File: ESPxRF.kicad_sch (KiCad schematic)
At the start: 22 parts, among them J1 Conn_Coaxial, J2 USB_C_Receptacle_USB2.0, U1 ESP32-S3, U2 NRF24L01, U3 NCP115ASN330T2G, U4 USBLC6-2SC6

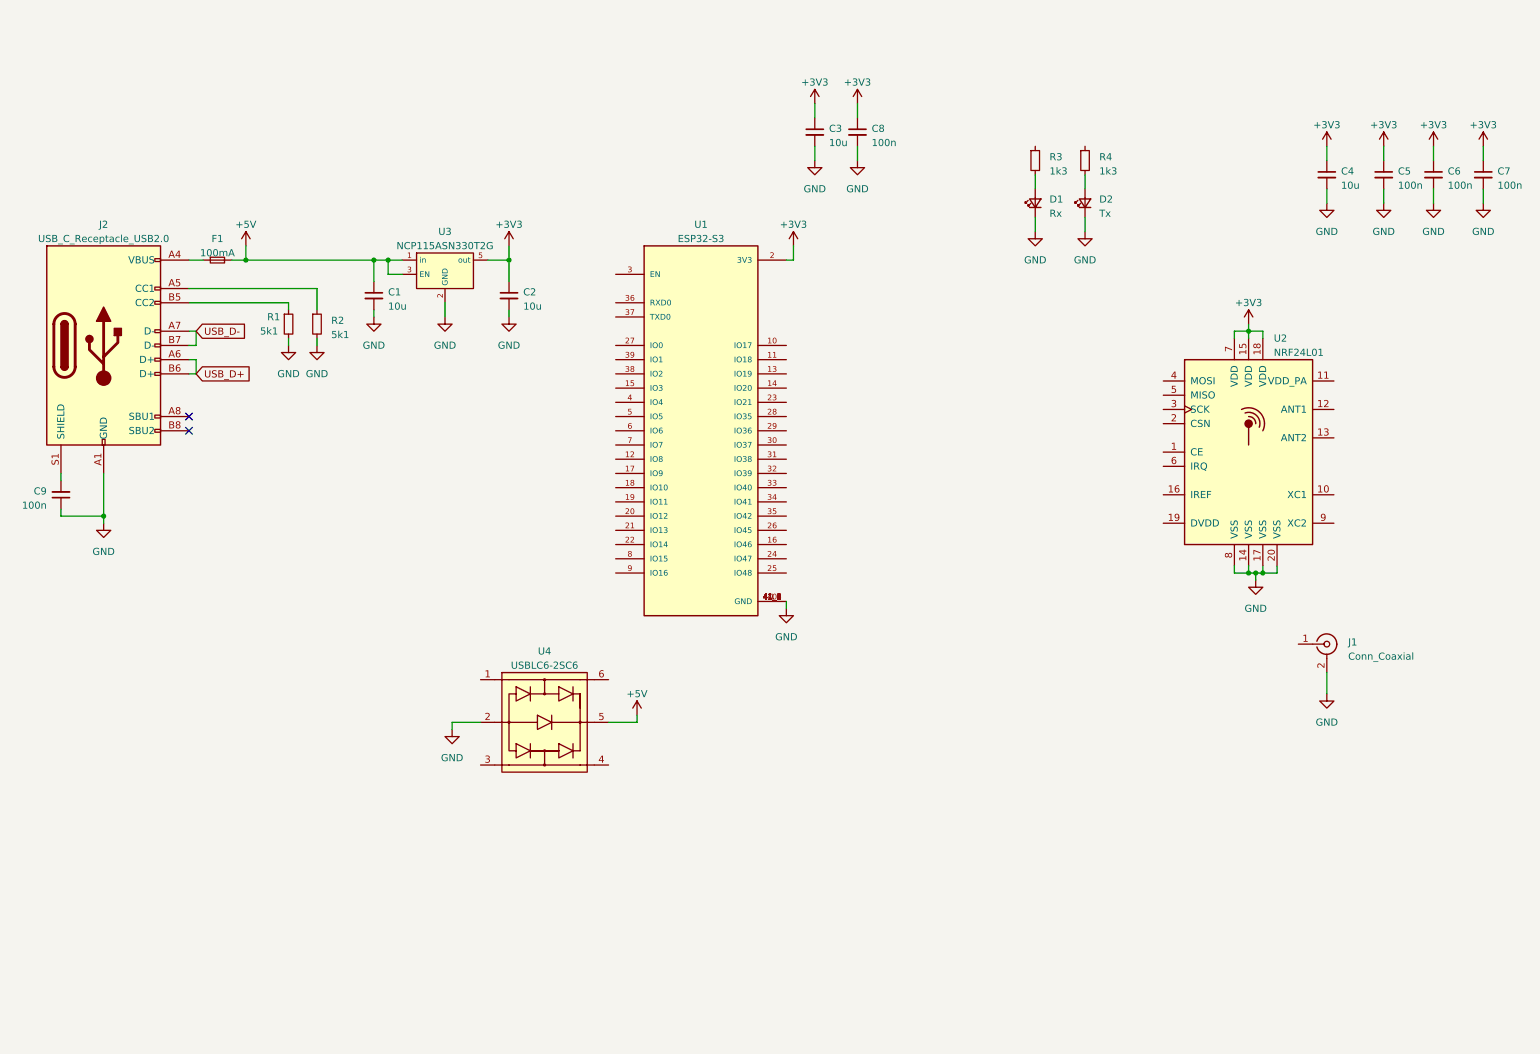
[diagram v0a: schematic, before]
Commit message: finished nrf schematic
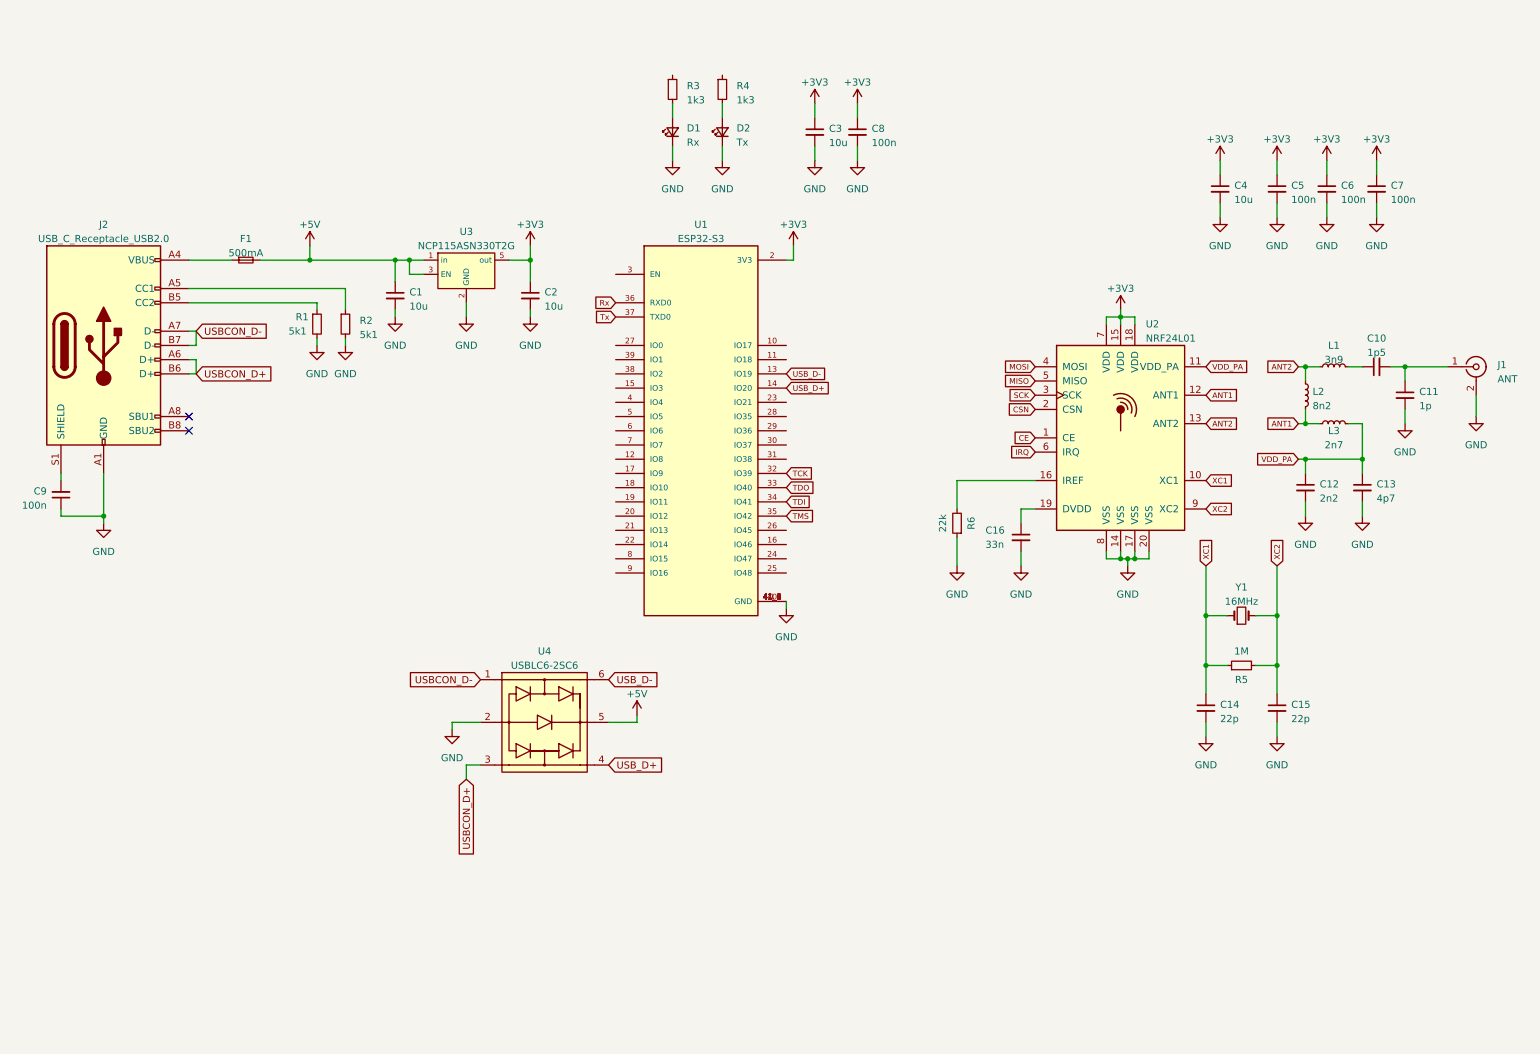
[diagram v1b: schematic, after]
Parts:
- added C10: 1p5, Capacitor_SMD:C_0402_1005Metric_Pad0.74x0.62mm_HandSolder, symbol Device:C_Small
- added C11: 1p, Capacitor_SMD:C_0402_1005Metric_Pad0.74x0.62mm_HandSolder, symbol Device:C_Small
- added C12: 2n2, Capacitor_SMD:C_0402_1005Metric_Pad0.74x0.62mm_HandSolder, symbol Device:C_Small
- added C13: 4p7, Capacitor_SMD:C_0402_1005Metric_Pad0.74x0.62mm_HandSolder, symbol Device:C_Small
- added C14, C15: 22p, Capacitor_SMD:C_0402_1005Metric_Pad0.74x0.62mm_HandSolder, symbol Device:C_Small
- added C16: 33n, Capacitor_SMD:C_0402_1005Metric_Pad0.74x0.62mm_HandSolder, symbol Device:C_Small
- added L1: 3n9, Inductor_SMD:L_0402_1005Metric_Pad0.77x0.64mm_HandSolder, symbol Device:L_Small
- added L2: 8n2, Inductor_SMD:L_0402_1005Metric_Pad0.77x0.64mm_HandSolder, symbol Device:L_Small
- added L3: 2n7, Inductor_SMD:L_0402_1005Metric_Pad0.77x0.64mm_HandSolder, symbol Device:L_Small
- added R5: 1M, Resistor_SMD:R_0603_1608Metric_Pad0.98x0.95mm_HandSolder, symbol Device:R_Small
- added R6: 22k, Resistor_SMD:R_0402_1005Metric_Pad0.72x0.64mm_HandSolder, symbol Device:R_Small
- added Y1: 16MHz, Crystal:Crystal_SMD_2520-4Pin_2.5x2.0mm, symbol Device:Crystal_Small
- F1: value 100mA -> 500mA
- J1: value Conn_Coaxial -> ANT
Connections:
- net GND: now also C11.2, C12.2, C13.2, C14.2, C15.2, C16.2, R6.1
- net USB_D+: now also U1.14 (IO20), U4.4; no longer J2.A6 (D+), J2.B6 (D+)
- net USB_D-: now also U1.13 (IO19), U4.6; no longer J2.A7 (D-), J2.B7 (D-)
- net USBCON_D-: now reaches U4.1
- net USBCON_D-: now also J2.A7 (D-), J2.B7 (D-)
- net USBCON_D+: now reaches U4.3
- net USBCON_D+: now also J2.A6 (D+), J2.B6 (D+)
- net at J1.1 (In): now also C10.2, C11.1
- net TCK: now reaches U1.32 (IO39)
- net TDO: now reaches U1.33 (IO40)
- net TDI: now reaches U1.34 (IO41)
- net TMS: now reaches U1.35 (IO42)
- net Rx: now reaches U1.36 (RXD0)
- net Tx: now reaches U1.37 (TXD0)
- net CE: now reaches U2.1 (CE)
- net XC1: now reaches U2.10 (XC1)
- net XC1: now also C14.1, R5.1, Y1.1
- net VDD_PA: now reaches U2.11 (VDD_PA)
- net VDD_PA: now also C12.1, C13.1, L3.2
- net ANT1: now reaches U2.12 (ANT1)
- net ANT1: now also L2.2, L3.1
- net ANT2: now reaches U2.13 (ANT2)
- net ANT2: now also L1.1, L2.1
- net at U2.16 (IREF): now also R6.2
- net at U2.19 (DVDD): now also C16.1
- net CSN: now reaches U2.2 (CSN)
- net SCK: now reaches U2.3 (SCK)
- net MOSI: now reaches U2.4 (MOSI)
- net MISO: now reaches U2.5 (MISO)
- net IRQ: now reaches U2.6 (IRQ)
- net XC2: now reaches U2.9 (XC2)
- net XC2: now also C15.1, R5.2, Y1.2
- new net: C10.1, L1.2
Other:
- moved on the sheet: C1, C2, C4, C5, C6, C7, D1, D2, F1, J1, R1, R2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

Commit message: nearly finished V1
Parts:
- removed C4: 10u, Capacitor_SMD:C_0603_1608Metric_Pad1.08x0.95mm_HandSolder, symbol Device:C_Small
- removed C9: 100n, Capacitor_SMD:C_0603_1608Metric_Pad1.08x0.95mm_HandSolder, symbol Device:C_Small
- removed Y1: 16MHz, Crystal:Crystal_SMD_2520-4Pin_2.5x2.0mm, symbol Device:Crystal_Small
- added C1: 10u, Capacitor_SMD:C_0603_1608Metric_Pad1.08x0.95mm_HandSolder, symbol Device:C_Small
- added C7, C8: 100n, Capacitor_SMD:C_0603_1608Metric_Pad1.08x0.95mm_HandSolder, symbol Device:C_Small
- added L1: 100R @ 100MHz, Inductor_SMD:L_0603_1608Metric_Pad1.05x0.95mm_HandSolder, symbol Device:L_Small
- added Y1: Crystal_GND24_Small, Crystal:Crystal_SMD_2520-4Pin_2.5x2.0mm, symbol Device:Crystal_GND24_Small
- C2: renamed from C5; footprint Capacitor_SMD:C_0603_1608Metric_Pad1.08x0.95mm_HandSolder -> Capacitor_SMD:C_0402_1005Metric_Pad0.74x0.62mm_HandSolder
- C3: renamed from C6; footprint Capacitor_SMD:C_0603_1608Metric_Pad1.08x0.95mm_HandSolder -> Capacitor_SMD:C_0402_1005Metric_Pad0.74x0.62mm_HandSolder
- C4: renamed from C7; footprint Capacitor_SMD:C_0603_1608Metric_Pad1.08x0.95mm_HandSolder -> Capacitor_SMD:C_0402_1005Metric_Pad0.74x0.62mm_HandSolder
- J2: renamed from J1; footprint Connector_Coaxial:SMA_Amphenol_132289_EdgeMount -> Connector_Coaxial:SMA_Samtec_SMA-J-P-X-ST-EM1_EdgeMount
- R6: renamed from R5; footprint Resistor_SMD:R_0603_1608Metric_Pad0.98x0.95mm_HandSolder -> Resistor_SMD:R_0402_1005Metric_Pad0.72x0.64mm_HandSolder
- renumbered C11 to C10, C12 to C11, C13 to C12, C3 to C13, C8 to C14, C16 to C15, C14 to C16, C15 to C17, C1 to C5, C2 to C6, C10 to C9, J2 to J1, L1 to L2, L2 to L3, L3 to L4, R3 to R1, R4 to R2, R1 to R3, R2 to R4, R6 to R5, U3 to U1, U4 to U3, U1 to U4
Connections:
- net +3V3: now also U4.3 (EN), C1.1, C8.1, L1.2; no longer C6.1, U1.5 (out)
- net CE: now also U4.26 (IO45)
- net CSN: now also U4.8 (IO15)
- net GND: now also C1.2, C7.2, C8.2, Y1.2, Y1.4
- net MISO: now also U4.20 (IO12)
- net MOSI: now also U4.21 (IO13)
- net SCK: now also U4.22 (IO14)
- net XC1: now also Y1.1
- net XC2: now also Y1.3
- net at R2.1: now also U4.10 (IO17)
- net at U4.9 (IO16): now also R1.1
- net Rx: no longer names the net of U4.36 (RXD0)
- net TCK: no longer names the net of U4.32 (IO39)
- net TDI: no longer names the net of U4.34 (IO41)
- net TDO: no longer names the net of U4.33 (IO40)
- net TMS: no longer names the net of U4.35 (IO42)
- net Tx: no longer names the net of U4.37 (TXD0)
- new net: C6.1, C7.1, L1.1, U1.5 (out)
- no-connect marks 2 -> 3
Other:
- moved on the sheet: C13, C14, C16, C17, D1, D2, R1, R2, R6, U3, U4

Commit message: added GND plane in two inner layers
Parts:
- U3: footprint SnapEda:SOT95P280X145-6N -> Package_TO_SOT_SMD:SOT-23-6_Handsoldering
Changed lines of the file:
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@@
       (effects (font (size 1.27 1.27)))
     )
-    (property "Footprint" "SnapEda:SOT95P280X145-6N" (at 26.67 109.22 0)
+    (property "Footprint" "Package_TO_SOT_SMD:SOT-23-6_Handsoldering" (at 26.67 109.22 0)
       (effects (font (size 1.27 1.27)) (justify left bottom) hide)
     )

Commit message: went through the DRC and assigned my own kicad libraries
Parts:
- U1: footprint NCP115ASN330T2G:NCP115ASN330T2G -> Package_TO_SOT_SMD:SOT-23-5_HandSoldering
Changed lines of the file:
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@@
       (effects (font (size 1.27 1.27)))
     )
-    (property "Footprint" "NCP115ASN330T2G:NCP115ASN330T2G" (at 95.25 49.53 0)
+    (property "Footprint" "Package_TO_SOT_SMD:SOT-23-5_HandSoldering" (at 95.25 49.53 0)
       (effects (font (size 1.27 1.27)) hide)
     )

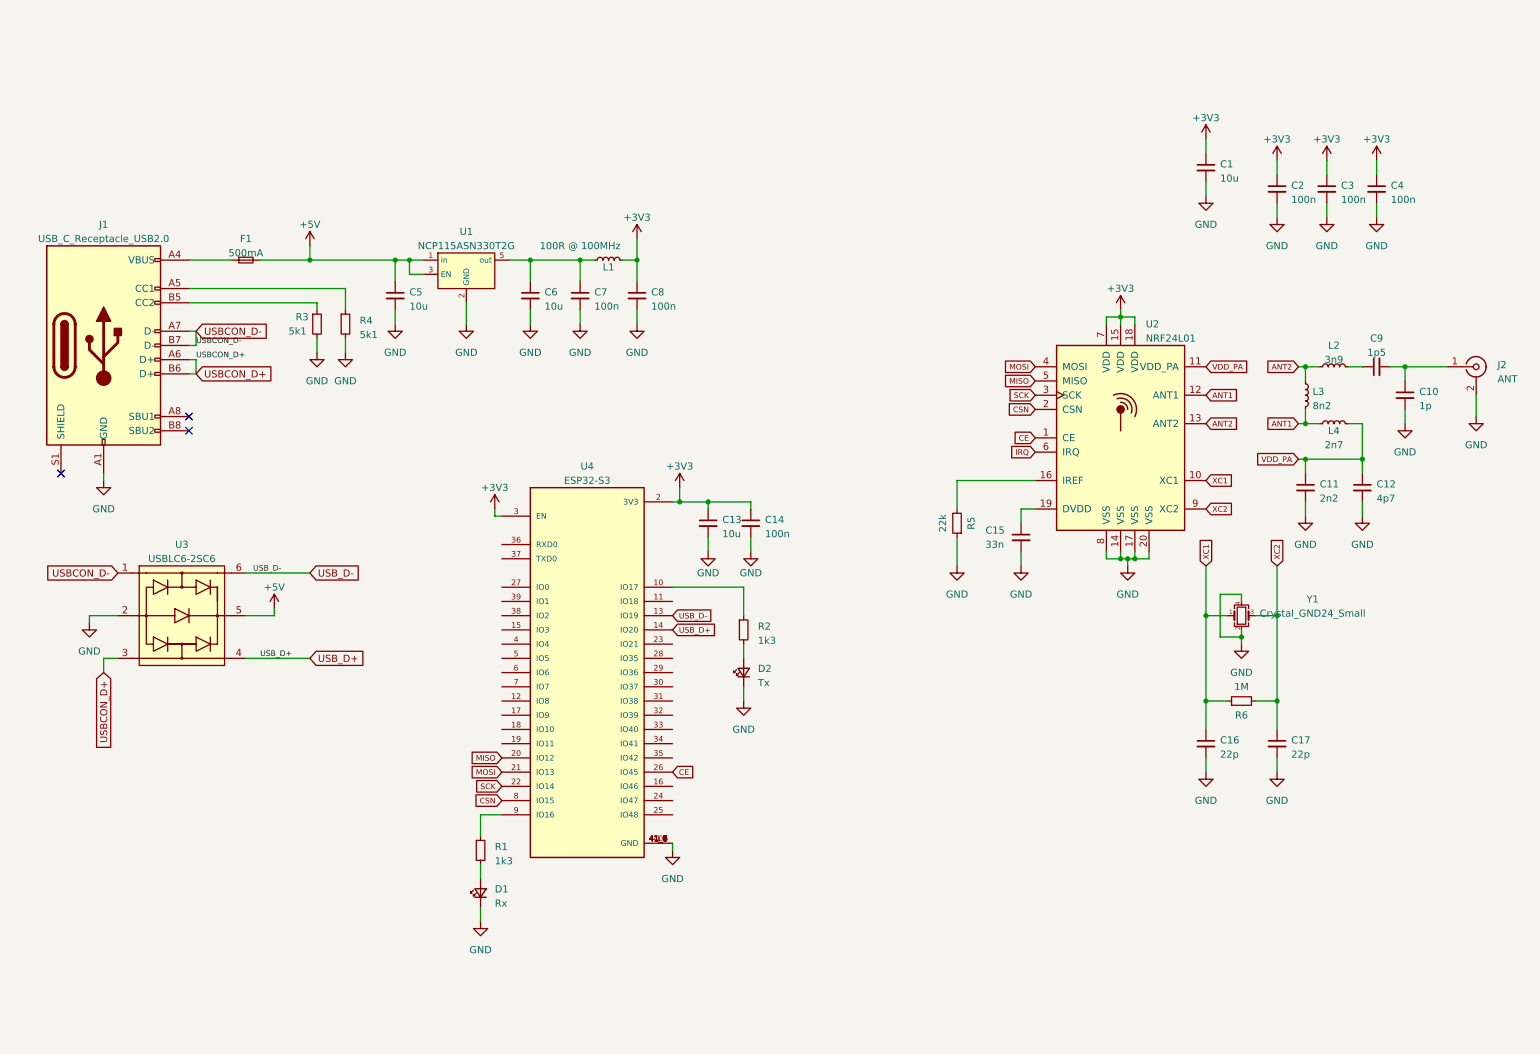
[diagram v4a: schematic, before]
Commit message: added jlc silkscreen tidied schematic
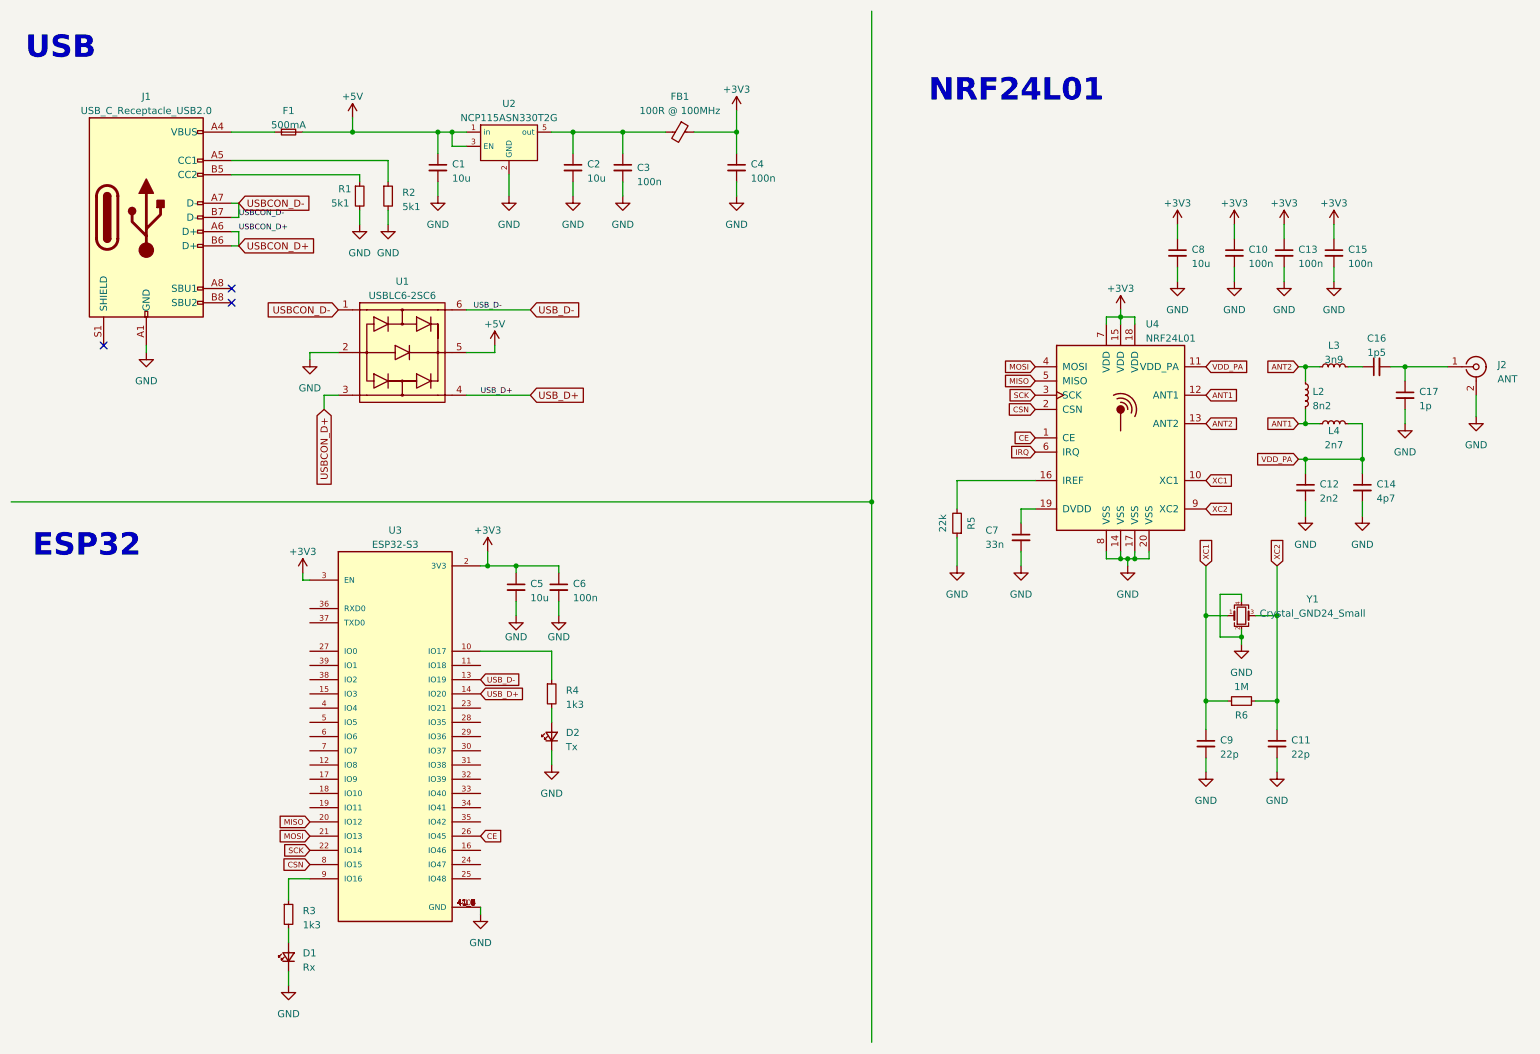
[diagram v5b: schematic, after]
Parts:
- removed L1: 100R @ 100MHz, Inductor_SMD:L_0603_1608Metric_Pad1.05x0.95mm_HandSolder, symbol Device:L_Small
- added FB1: 100R @ 100MHz, Inductor_SMD:L_0603_1608Metric_Pad1.05x0.95mm_HandSolder, symbol Device:FerriteBead_Small
- renumbered C5 to C1, C2 to C10, C17 to C11, C11 to C12, C3 to C13, C12 to C14, C4 to C15, C9 to C16, C10 to C17, C6 to C2, C7 to C3, C8 to C4, C13 to C5, C14 to C6, C15 to C7, C1 to C8, C16 to C9, L3 to L2, L2 to L3, R3 to R1, R4 to R2, R1 to R3, R2 to R4, U3 to U1, U1 to U2, U4 to U3, U2 to U4
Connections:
- net +3V3: now also FB1.1
- net at C2.1, C3.1, U2.5 (out): now also FB1.2
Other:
- note added: "ESP32"
- note added: "NRF24L01"
- note added: "USB"
- company: (none) -> Thomas S. Perri
- title: (none) -> ESP_RFLINK
- moved on the sheet: C1, C10, C13, C15, C2, C3, C4, C5, C6, C8, D1, D2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
